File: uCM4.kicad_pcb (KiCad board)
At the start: 2 copper layers, 55 x 40 mm, 30 parts, among them J1 Conn_01x03, J2 Ethernet, J3 Micro_SD_Card, J4 USB_B_Micro, SW1 SW_DIP_x01, SW2 SW_DIP_x01, U1 RT9742GGJ5, U2 74LVC1G07, U3 TPD4EUSB30

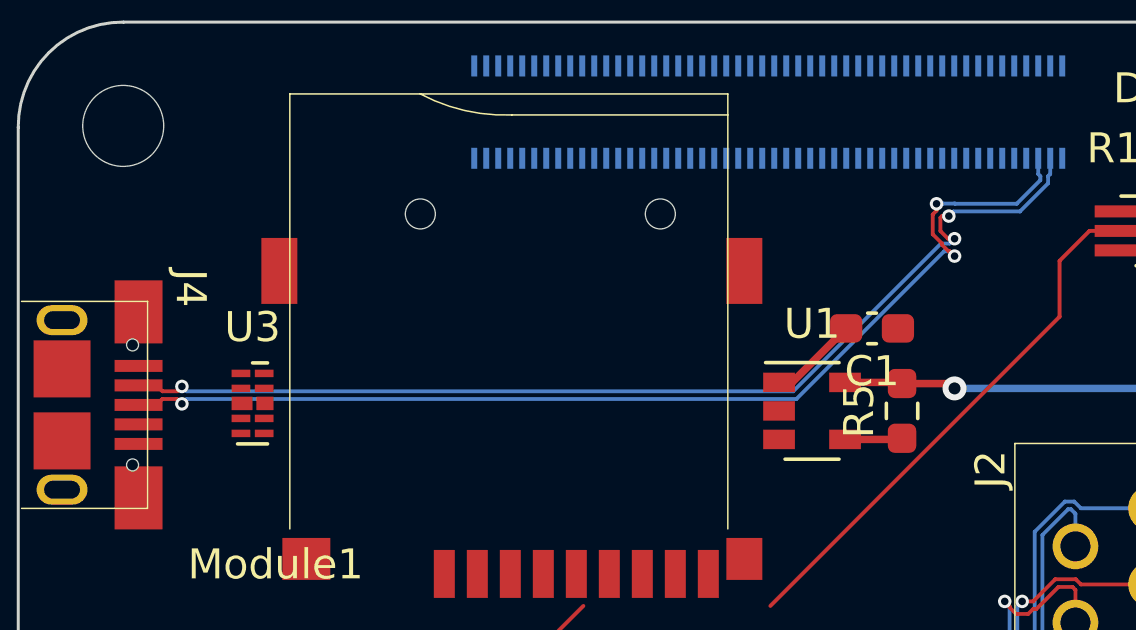
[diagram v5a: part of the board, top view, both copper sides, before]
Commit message: Adjust USB traces
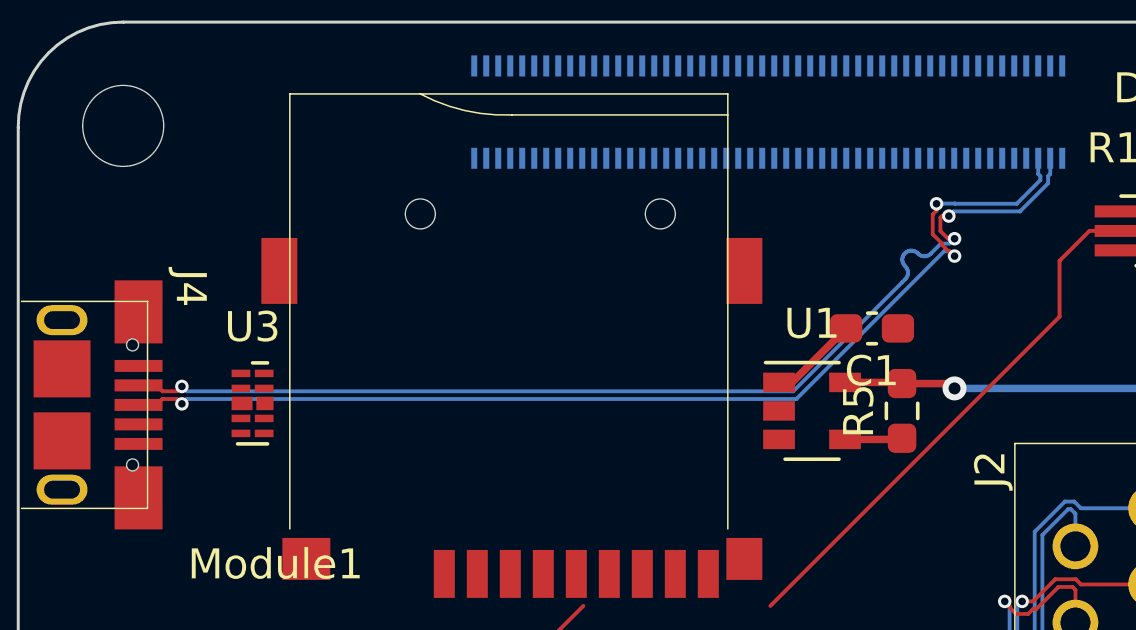
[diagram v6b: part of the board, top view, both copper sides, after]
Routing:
- net /USB_N: track 35.5 -> 36.2 mm
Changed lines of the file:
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@@
   (via (at 169 68.51) (size 0.45) (drill 0.25) (layers "F.Cu" "B.Cu") (net 165))
   (via (at 143.245002 73.435) (size 0.45) (drill 0.25) (layers "F.Cu" "B.Cu") (net 165))
+  (segment (start 167.345607 68.994136) (end 167.303721 69.046658) (width 0.127) (layer "B.Cu") (net 165))
+  (segment (start 167.274574 69.305351) (end 167.303721 69.365877) (width 0.127) (layer "B.Cu") (net 165))
+  (segment (start 167.431639 69.744615) (end 167.402492 69.805141) (width 0.127) (layer "B.Cu") (net 165))
+  (segment (start 167.398129 68.95225) (end 167.345607 68.994136) (width 0.127) (layer "B.Cu") (net 165))
+  (segment (start 167.717348 68.95225) (end 167.656822 68.923103) (width 0.127) (layer "B.Cu") (net 165))
+  (segment (start 168.8385 68.6715) (end 168.546772 68.6715) (width 0.127) (layer "B.Cu") (net 165))
+  (segment (start 167.591328 68.908154) (end 167.524149 68.908154) (width 0.127) (layer "B.Cu") (net 165))
+  (segment (start 168.546772 68.6715) (end 168.209136 69.009136) (width 0.127) (layer "B.Cu") (net 165))
+  (segment (start 167.458655 68.923103) (end 167.398129 68.95225) (width 0.127) (layer "B.Cu") (net 165))
   (segment (start 168.962793 67.602585) (end 171.179143 67.602585) (width 0.127) (layer "B.Cu") (net 165))
+  (segment (start 167.446588 69.679121) (end 167.431639 69.744615) (width 0.127) (layer "B.Cu") (net 165))
   (segment (start 171.179143 67.602585) (end 172.1175 66.664228) (width 0.127) (layer "B.Cu") (net 165))
-  (segment (start 143.245002 73.435) (end 143.406502 73.5965) (width 0.127) (layer "B.Cu") (net 165))
+  (segment (start 167.656822 68.923103) (end 167.591328 68.908154) (width 0.127) (layer "B.Cu") (net 165))
+  (segment (start 167.769871 68.994136) (end 167.717348 68.95225) (width 0.127) (layer "B.Cu") (net 165))
+  (segment (start 167.254542 69.96373) (end 163.621772 73.5965) (width 0.127) (layer "B.Cu") (net 165))
+  (segment (start 167.360607 69.857664) (end 167.254542 69.96373) (width 0.127) (layer "B.Cu") (net 165))
+  (segment (start 168.096087 69.080168) (end 168.030593 69.095117) (width 0.127) (layer "B.Cu") (net 165))
+  (segment (start 167.431639 69.546448) (end 167.446588 69.611942) (width 0.127) (layer "B.Cu") (net 165))
+  (segment (start 167.345607 69.4184) (end 167.360606 69.433399) (width 0.127) (layer "B.Cu") (net 165))
+  (segment (start 163.621772 73.5965) (end 143.406502 73.5965) (width 0.127) (layer "B.Cu") (net 165))
+  (segment (start 167.303721 69.046658) (end 167.274574 69.107184) (width 0.127) (layer "B.Cu") (net 165))
+  (segment (start 167.837394 69.051021) (end 167.784871 69.009136) (width 0.127) (layer "B.Cu") (net 165))
+  (segment (start 143.406502 73.5965) (end 143.245002 73.435) (width 0.127) (layer "B.Cu") (net 165))
+  (segment (start 167.446588 69.611942) (end 167.446588 69.679121) (width 0.127) (layer "B.Cu") (net 165))
+  (segment (start 167.259625 69.172678) (end 167.259625 69.239857) (width 0.127) (layer "B.Cu") (net 165))
+  (segment (start 167.360606 69.433399) (end 167.402492 69.485922) (width 0.127) (layer "B.Cu") (net 165))
   (segment (start 168.809671 67.755707) (end 168.962793 67.602585) (width 0.127) (layer "B.Cu") (net 165))
+  (segment (start 167.303721 69.365877) (end 167.345607 69.4184) (width 0.127) (layer "B.Cu") (net 165))
   (segment (start 172.1175 66.664228) (end 172.1175 66.426501) (width 0.127) (layer "B.Cu") (net 165))
+  (segment (start 167.274574 69.107184) (end 167.259625 69.172678) (width 0.127) (layer "B.Cu") (net 165))
+  (segment (start 167.89792 69.080168) (end 167.837394 69.051021) (width 0.127) (layer "B.Cu") (net 165))
   (segment (start 172.1175 66.426501) (end 172.189 66.355001) (width 0.127) (layer "B.Cu") (net 165))
-  (segment (start 168.8385 68.6715) (end 169 68.51) (width 0.127) (layer "B.Cu") (net 165))
   (segment (start 172.189 66.355001) (end 172.189 65.83) (width 0.127) (layer "B.Cu") (net 165))
-  (segment (start 163.621772 73.5965) (end 168.546772 68.6715) (width 0.127) (layer "B.Cu") (net 165))
-  (segment (start 143.406502 73.5965) (end 163.621772 73.5965) (width 0.127) (layer "B.Cu") (net 165))
-  (segment (start 168.546772 68.6715) (end 168.8385 68.6715) (width 0.127) (layer "B.Cu") (net 165))
+  (segment (start 167.402492 69.485922) (end 167.431639 69.546448) (width 0.127) (layer "B.Cu") (net 165))
+  (segment (start 167.259625 69.239857) (end 167.274574 69.305351) (width 0.127) (layer "B.Cu") (net 165))
+  (segment (start 167.524149 68.908154) (end 167.458655 68.923103) (width 0.127) (layer "B.Cu") (net 165))
+  (segment (start 169 68.51) (end 168.8385 68.6715) (width 0.127) (layer "B.Cu") (net 165))
+  (segment (start 167.402492 69.805141) (end 167.360607 69.857664) (width 0.127) (layer "B.Cu") (net 165))
+  (segment (start 167.963414 69.095117) (end 167.89792 69.080168) (width 0.127) (layer "B.Cu") (net 165))
+  (segment (start 168.030593 69.095117) (end 167.963414 69.095117) (width 0.127) (layer "B.Cu") (net 165))
+  (segment (start 168.156613 69.051021) (end 168.096087 69.080168) (width 0.127) (layer "B.Cu") (net 165))
+  (segment (start 168.209136 69.009136) (end 168.156613 69.051021) (width 0.127) (layer "B.Cu") (net 165))
+  (segment (start 167.784871 69.009136) (end 167.769871 68.994136) (width 0.127) (layer "B.Cu") (net 165))
   (zone (net 0) (net_name "") (layers F&B.Cu) (name "Wireless Cutout") (hatch edge 0.508)
     (connect_pads (clearance 0))

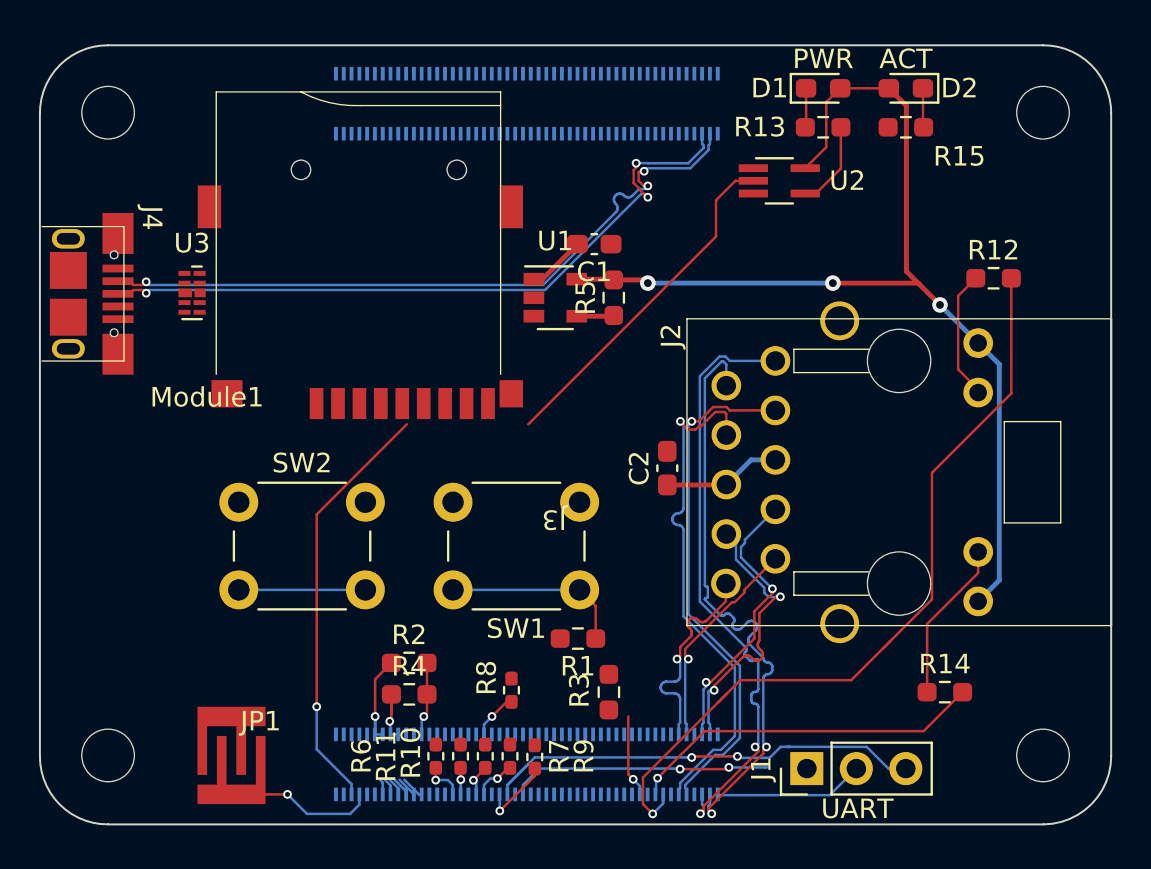
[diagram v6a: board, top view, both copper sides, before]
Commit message: Start routing power buses
Most likely not the target way to do that, but just to indicate the
problem.
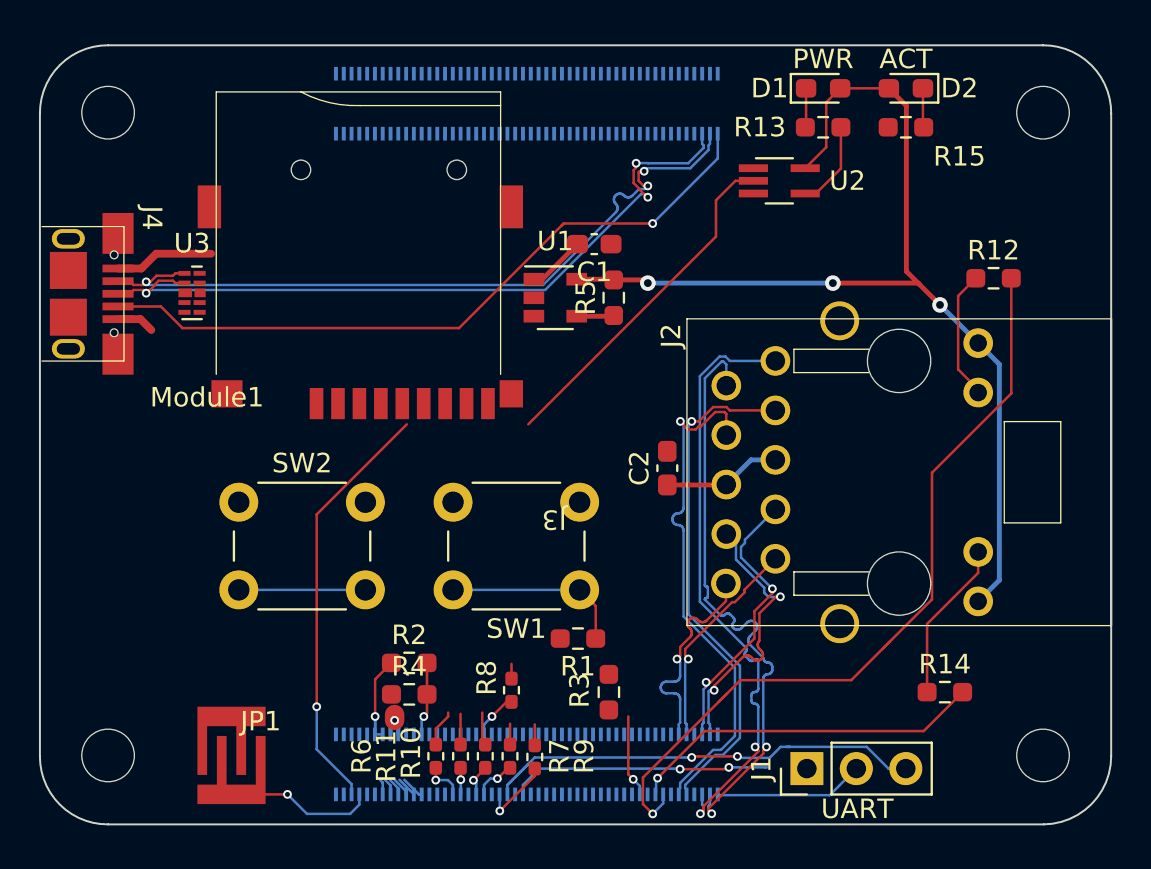
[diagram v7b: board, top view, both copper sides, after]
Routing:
- net Net-(J4-Pad4): track 0.00 -> 36.1 mm, vias 0 -> 1
- net +5V: track 5.86 -> 11.0 mm
- net /USB_P: track 36.2 -> 38.5 mm
- net /USB_N: track 36.2 -> 38.3 mm
- net GND: track 7.68 -> 9.62 mm
- net Net-(J3-Pad1): track 0.00 -> 1.91 mm
- net Net-(J3-Pad7): track 0.00 -> 1.71 mm
- net Net-(J3-Pad8): track 0.00 -> 1.58 mm
- net +3V3: track 57.7 -> 56.1 mm
- net Net-(J3-Pad5): track 0.00 -> 1.08 mm
- net Net-(J3-Pad2): track 0.00 -> 1.07 mm
- net Net-(J3-Pad3): track 0.00 -> 0.76 mm

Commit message: Make main power line
Base on calculator calculations. It should stand 2A current. However the
line near connector can have only 1.2 A.
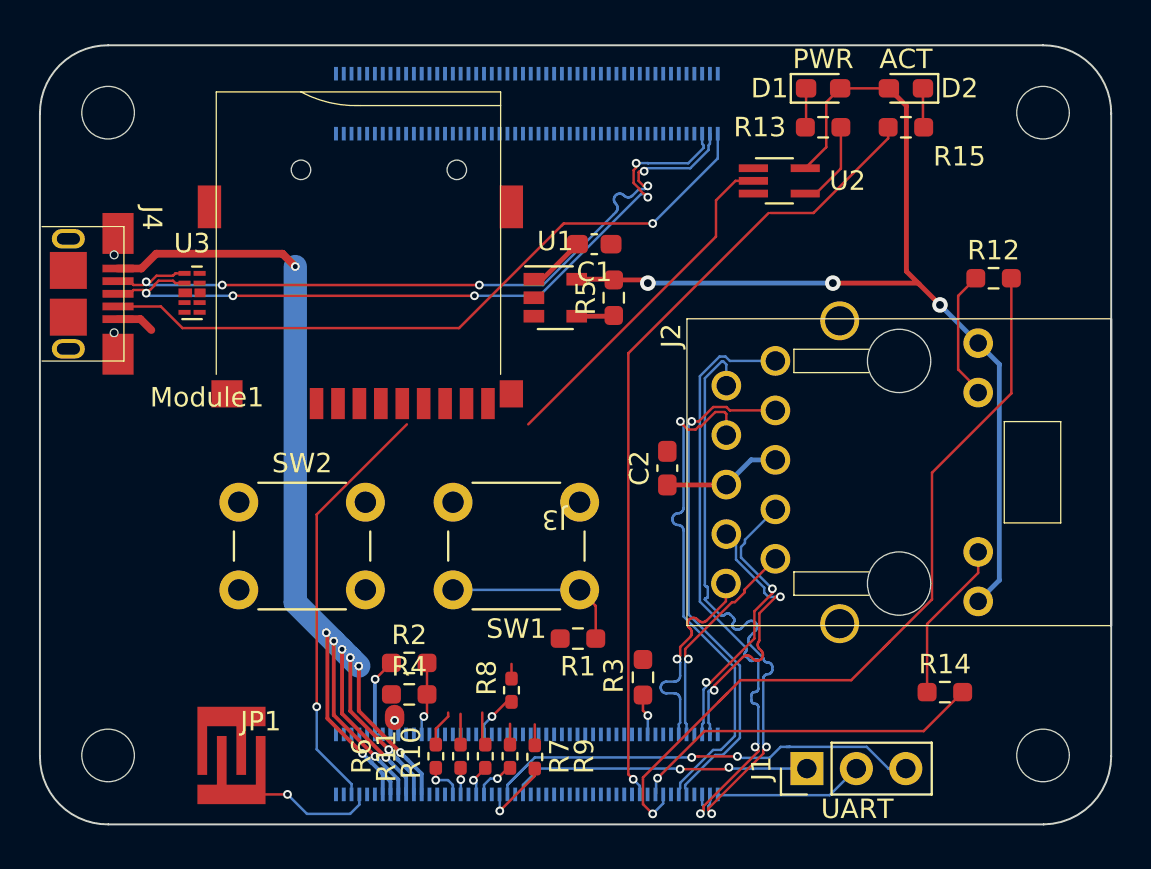
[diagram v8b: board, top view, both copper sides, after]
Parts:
- moved R3 1.91 mm to (168.8, 93.7)
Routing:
- net +5V: track 11.0 -> 77.2 mm, vias 0 -> 11
- net Net-(Module1-Pad21): track 4.24 -> 41.3 mm
- net Net-(Module1-Pad99): track 6.50 -> 0.00 mm
- net Net-(Module1-Pad20): track 0.00 -> 2.13 mm, vias 0 -> 1
- net Net-(J1-Pad1): track 13.5 -> 15.6 mm
- net +1V8: track 4.95 -> 4.44 mm
- net /USB_P: track 38.5 -> 38.6 mm, vias 3 -> 5
- net /USB_N: vias 3 -> 5
